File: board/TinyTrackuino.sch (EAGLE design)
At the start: 16 parts, among them M2 HX1, Q1 PMV20XN, PMV16UN, etc, U1 LM60 int, X1 BU-SMA-V, X2 Vin, X3 LM60 ext, X4 Buzzer, X5 SM06B-SRSS-TB

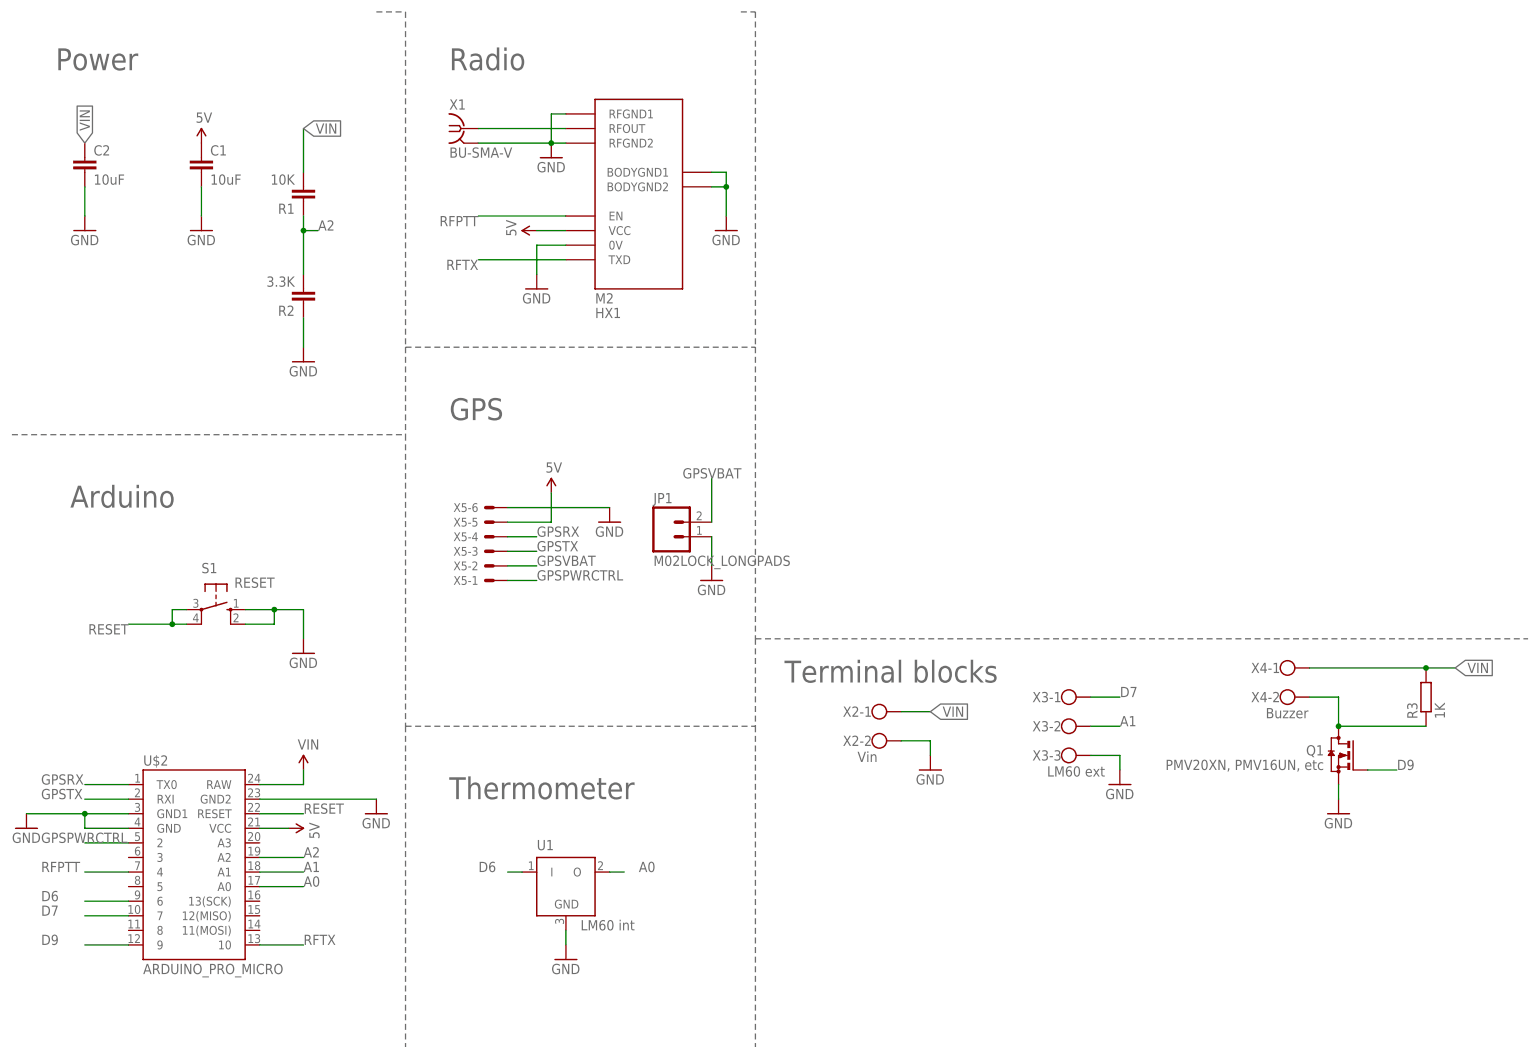
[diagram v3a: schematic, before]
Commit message: Using 3.5mm screw terminals instead of 5mm
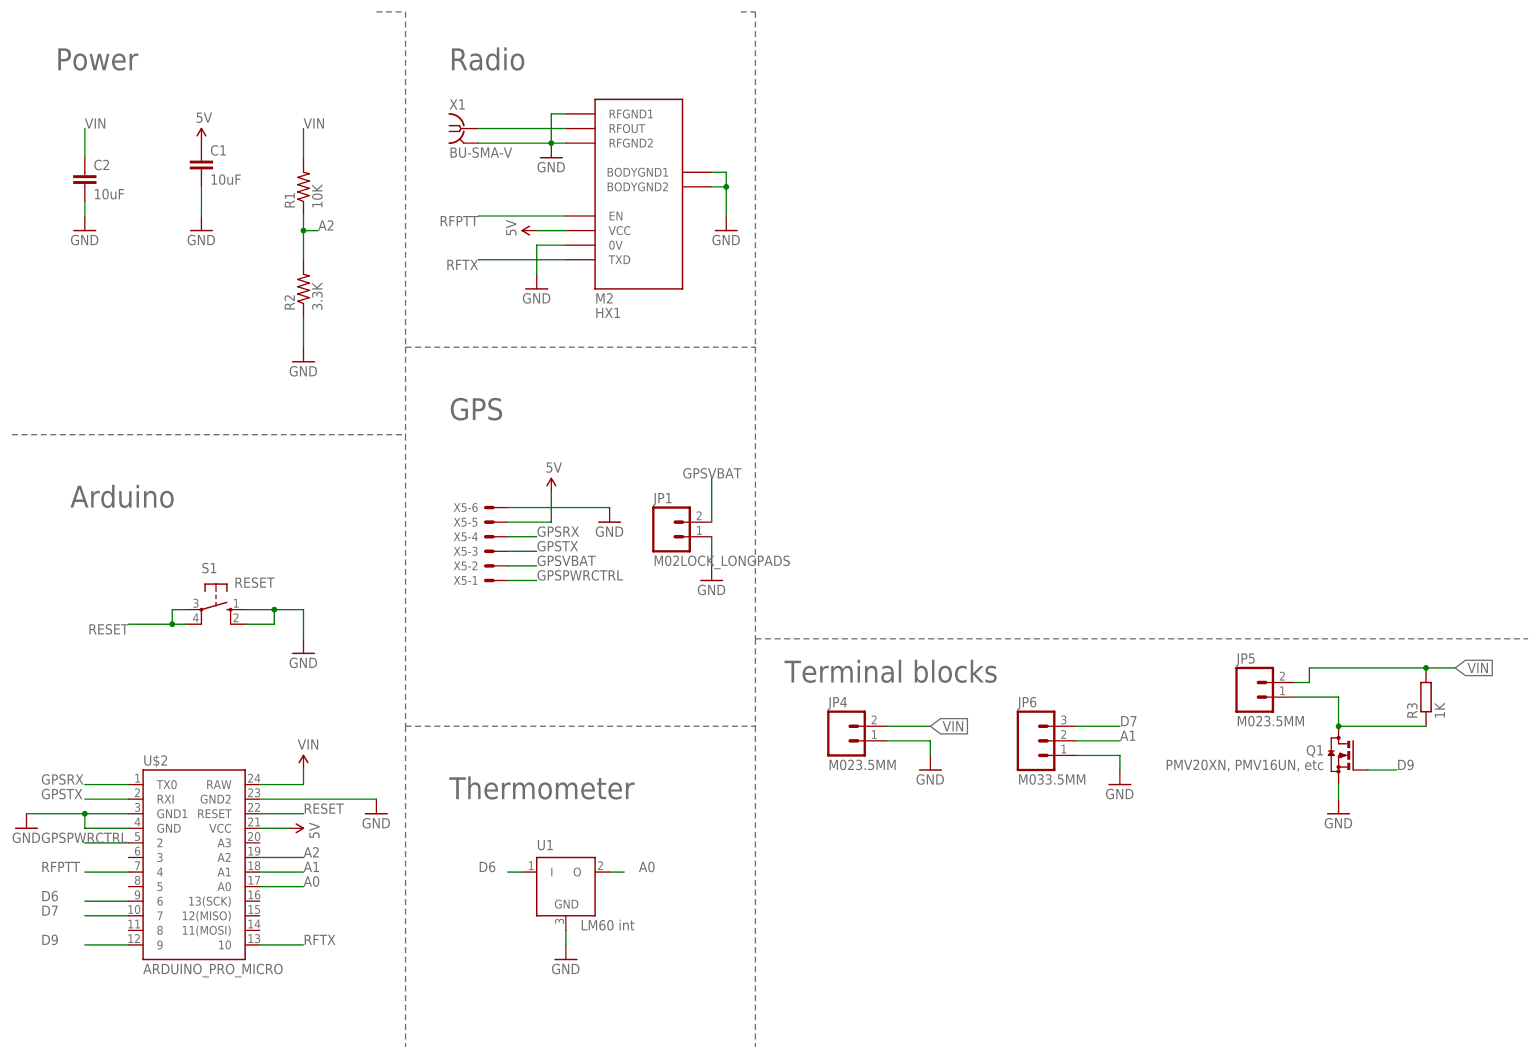
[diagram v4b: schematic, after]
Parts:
- removed X2: Vin, con-wago-500:W237-102
- removed X3: LM60 ext, con-wago-500:W237-103
- removed X4: Buzzer, con-wago-500:W237-102
- added JP4, JP5: M023.5MM, SparkFun-Connectors:M023.5MM
- added JP6: M033.5MM, SparkFun-Connectors:M03SCREW
- R1, R2: device SparkFun-Passives:CAP0603-CAP -> SparkFun-Passives:RESISTOR0603-RES
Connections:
- net A1: now also JP6.2; no longer X3-2.KL
- net D7: now also JP6.3; no longer X3-1.KL
- net GND: now also JP4.1, JP6.1; no longer X2-2.KL, X3-3.KL
- net N$1: now also JP5.1; no longer X4-2.KL
- net VIN: now also JP4.2, JP5.2; no longer X2-1.KL, X4-1.KL
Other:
- moved on the sheet: C2
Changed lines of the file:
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@@
 <part name="U1" library="trackuino" deviceset="LM60" device="" value="LM60 int"/>
 <part name="X1" library="con-coax" deviceset="BU-SMA-V" device=""/>
-<part name="X2" library="con-wago-500" deviceset="W237-102" device="" value="Vin"/>
-<part name="X3" library="con-wago-500" deviceset="W237-103" device="" value="LM60 ext"/>
 <part name="GND12" library="supply1" deviceset="GND" device=""/>
 <part name="GND13" library="supply1" deviceset="GND" device=""/>
-<part name="X4" library="con-wago-500" deviceset="W237-102" device="" value="Buzzer"/>
 <part name="GND14" library="supply1" deviceset="GND" device=""/>
 <part name="GND20" library="supply1" deviceset="GND" device=""/>
-<part name="R1" library="SparkFun-Passives" deviceset="CAP" device="0603-CAP" value="10K"/>
-<part name="R2" library="SparkFun-Passives" deviceset="CAP" device="0603-CAP" value="3.3K"/>
+<part name="R1" library="SparkFun-Passives" deviceset="RESISTOR" device="0603-RES" value="10K"/>
+<part name="R2" library="SparkFun-Passives" deviceset="RESISTOR" device="0603-RES" value="3.3K"/>
 <part name="GND21" library="supply1" deviceset="GND" device=""/>
 <part name="Q1" library="transistor-small-signal" deviceset="BSS123" device="" value="PMV20XN, PMV16UN, etc"/>
@@
 <part name="SUPPLY5" library="SparkFun-Aesthetics" deviceset="5V" device=""/>
 <part name="X5" library="con-jst2" deviceset="?M06B-SRSS-TB" device="S"/>
+<part name="JP4" library="SparkFun-Connectors" deviceset="M02" device="3.5MM"/>
+<part name="JP5" library="SparkFun-Connectors" deviceset="M02" device="3.5MM"/>
+<part name="JP6" library="SparkFun-Connectors" deviceset="M03" device="SCREW" value="M033.5MM"/>
 </parts>
 <sheets>
@@
 <instance part="GND10" gate="1" x="33.02" y="142.24"/>
 <instance part="C1" gate="G$1" x="33.02" y="152.4"/>
-<instance part="C2" gate="G$1" x="12.7" y="152.4"/>
+<instance part="C2" gate="G$1" x="12.7" y="149.86"/>
 <instance part="GND" gate="1" x="93.98" y="154.94"/>
 <instance part="FRAME1" gate="G$1" x="0" y="0"/>
@@
 <instance part="U1" gate="G$1" x="96.52" y="27.94"/>
 <instance part="X1" gate="G$1" x="78.74" y="160.02"/>
-<instance part="X2" gate="-1" x="149.86" y="58.42"/>
-<instance part="X2" gate="-2" x="149.86" y="53.34"/>
-<instance part="X3" gate="-1" x="182.88" y="60.96"/>
-<instance part="X3" gate="-2" x="182.88" y="55.88"/>
-<instance part="X3" gate="-3" x="182.88" y="50.8"/>
 <instance part="GND12" gate="1" x="160.02" y="48.26"/>
 <instance part="GND13" gate="1" x="193.04" y="45.72"/>
-<instance part="X4" gate="-1" x="220.98" y="66.04"/>
-<instance part="X4" gate="-2" x="220.98" y="60.96"/>
 <instance part="GND14" gate="1" x="231.14" y="40.64"/>
 <instance part="GND20" gate="1" x="124.46" y="142.24"/>
-<instance part="R1" gate="G$1" x="50.8" y="149.86" rot="R180"/>
-<instance part="R2" gate="G$1" x="50.8" y="132.08" rot="R180"/>
+<instance part="R1" gate="G$1" x="50.8" y="149.86" rot="R90"/>
+<instance part="R2" gate="G$1" x="50.8" y="132.08" rot="R90"/>
 <instance part="GND21" gate="1" x="50.8" y="119.38"/>
 <instance part="Q1" gate="G$1" x="231.14" y="50.8" rot="MR0"/>
@@
 <instance part="X5" gate="-5" x="83.82" y="91.44" rot="R180"/>
 <instance part="X5" gate="-6" x="83.82" y="93.98" rot="R180"/>
+<instance part="JP4" gate="G$1" x="144.78" y="53.34"/>
+<instance part="JP5" gate="G$1" x="215.9" y="60.96"/>
+<instance part="JP6" gate="G$1" x="177.8" y="53.34"/>
 </instances>
 <busses>
@@
 <net name="GND" class="0">
 <segment>
-<wire x1="12.7" y1="149.86" x2="12.7" y2="144.78" width="0.1524" layer="91"/>
+<wire x1="12.7" y1="147.32" x2="12.7" y2="144.78" width="0.1524" layer="91"/>
 <pinref part="GND9" gate="1" pin="GND"/>
 <pinref part="C2" gate="G$1" pin="2"/>
@@
 </segment>
 <segment>
-<wire x1="154.94" y1="53.34" x2="160.02" y2="53.34" width="0.1524" layer="91"/>
+<wire x1="152.4" y1="53.34" x2="160.02" y2="53.34" width="0.1524" layer="91"/>
 <wire x1="160.02" y1="53.34" x2="160.02" y2="50.8" width="0.1524" layer="91"/>
-<pinref part="X2" gate="-2" pin="KL"/>
 <pinref part="GND12" gate="1" pin="GND"/>
-</segment>
-<segment>
-<wire x1="187.96" y1="50.8" x2="193.04" y2="50.8" width="0.1524" layer="91"/>
+<pinref part="JP4" gate="G$1" pin="1"/>
+</segment>
+<segment>
+<wire x1="185.42" y1="50.8" x2="193.04" y2="50.8" width="0.1524" layer="91"/>
 <wire x1="193.04" y1="50.8" x2="193.04" y2="48.26" width="0.1524" layer="91"/>
-<pinref part="X3" gate="-3" pin="KL"/>
 <pinref part="GND13" gate="1" pin="GND"/>
+<pinref part="JP6" gate="G$1" pin="1"/>
 </segment>
 <segment>
@@
 <net name="VIN" class="0">
 <segment>
-<wire x1="154.94" y1="58.42" x2="160.02" y2="58.42" width="0.1524" layer="91"/>
-<label x="160.02" y="58.42" size="1.778" layer="95" xref="yes"/>
-<pinref part="X2" gate="-1" pin="KL"/>
-</segment>
-<segment>
-<wire x1="50.8" y1="152.4" x2="50.8" y2="160.02" width="0.1524" layer="91"/>
-<label x="50.8" y="160.02" size="1.778" layer="95" xref="yes"/>
-<pinref part="R1" gate="G$1" pin="2"/>
+<wire x1="152.4" y1="55.88" x2="160.02" y2="55.88" width="0.1524" layer="91"/>
+<label x="160.02" y="55.88" size="1.778" layer="95" xref="yes"/>
+<pinref part="JP4" gate="G$1" pin="2"/>
 </segment>
 <segment>
@@
 <junction x="246.38" y="66.04"/>
 <label x="251.46" y="66.04" size="1.778" layer="95" xref="yes"/>
-<pinref part="X4" gate="-1" pin="KL"/>
 <pinref part="R3" gate="G$1" pin="2"/>
-</segment>
-<segment>
-<pinref part="C2" gate="G$1" pin="1"/>
-<label x="12.7" y="157.48" size="1.778" layer="95" rot="R90" xref="yes"/>
+<pinref part="JP5" gate="G$1" pin="2"/>
+<wire x1="223.52" y1="63.5" x2="226.06" y2="63.5" width="0.1524" layer="91"/>
+<wire x1="226.06" y1="63.5" x2="226.06" y2="66.04" width="0.1524" layer="91"/>
 </segment>
 <segment>
@@
 <wire x1="50.8" y1="45.72" x2="50.8" y2="48.26" width="0.1524" layer="91"/>
 </segment>
+<segment>
+<pinref part="C2" gate="G$1" pin="1"/>
+<wire x1="12.7" y1="160.02" x2="12.7" y2="154.94" width="0.1524" layer="91"/>
+<label x="12.7" y="160.02" size="1.778" layer="95"/>
+</segment>
+<segment>
+<pinref part="R1" gate="G$1" pin="2"/>
+<wire x1="50.8" y1="154.94" x2="50.8" y2="160.02" width="0.1524" layer="91"/>
+<label x="50.8" y="160.02" size="1.778" layer="95"/>
+</segment>
 </net>
 <net name="A0" class="0">
@@
 <net name="A1" class="0">
 <segment>
-<wire x1="187.96" y1="55.88" x2="193.04" y2="55.88" width="0.1524" layer="91"/>
-<label x="193.04" y="55.88" size="1.778" layer="95"/>
-<pinref part="X3" gate="-2" pin="KL"/>
+<wire x1="185.42" y1="53.34" x2="193.04" y2="53.34" width="0.1524" layer="91"/>
+<label x="193.04" y="53.34" size="1.778" layer="95"/>
+<pinref part="JP6" gate="G$1" pin="2"/>
 </segment>
 <segment>
@@
 <segment>
 <wire x1="50.8" y1="144.78" x2="50.8" y2="142.24" width="0.1524" layer="91"/>
-<wire x1="50.8" y1="142.24" x2="50.8" y2="134.62" width="0.1524" layer="91"/>
+<wire x1="50.8" y1="142.24" x2="50.8" y2="137.16" width="0.1524" layer="91"/>
 <wire x1="50.8" y1="142.24" x2="53.34" y2="142.24" width="0.1524" layer="91"/>
 <junction x="50.8" y="142.24"/>
@@
 <net name="D7" class="0">
 <segment>
-<wire x1="187.96" y1="60.96" x2="193.04" y2="60.96" width="0.1524" layer="91"/>
-<label x="193.04" y="60.96" size="1.778" layer="95"/>
-<pinref part="X3" gate="-1" pin="KL"/>
+<wire x1="185.42" y1="55.88" x2="193.04" y2="55.88" width="0.1524" layer="91"/>
+<label x="193.04" y="55.88" size="1.778" layer="95"/>
+<pinref part="JP6" gate="G$1" pin="3"/>
 </segment>
 <segment>
@@
 <net name="N$1" class="0">
 <segment>
-<wire x1="226.06" y1="60.96" x2="231.14" y2="60.96" width="0.1524" layer="91"/>
+<wire x1="223.52" y1="60.96" x2="231.14" y2="60.96" width="0.1524" layer="91"/>
 <wire x1="231.14" y1="60.96" x2="231.14" y2="55.88" width="0.1524" layer="91"/>
 <wire x1="231.14" y1="55.88" x2="246.38" y2="55.88" width="0.1524" layer="91"/>
 <junction x="231.14" y="55.88"/>
-<pinref part="X4" gate="-2" pin="KL"/>
 <pinref part="Q1" gate="G$1" pin="D"/>
 <pinref part="R3" gate="G$1" pin="1"/>
-</segment>
-</net>
+<pinref part="JP5" gate="G$1" pin="1"/>
+</segment>
+</net>

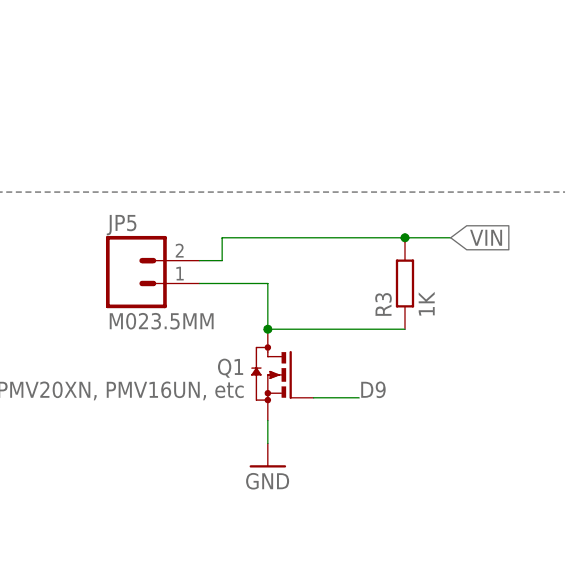
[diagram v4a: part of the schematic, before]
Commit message: Moving Vin to edge of board
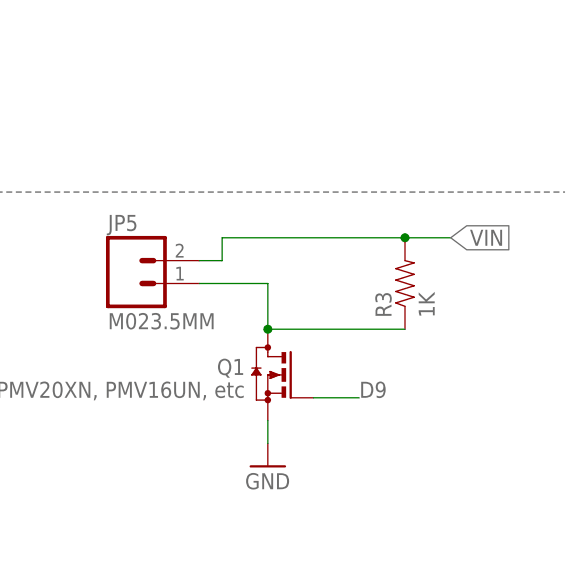
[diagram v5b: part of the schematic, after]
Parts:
- R3: device resistor:R-EU_R1206 -> SparkFun-Passives:RESISTOR0603-RES
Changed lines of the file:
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@@
 <part name="GND21" library="supply1" deviceset="GND" device=""/>
 <part name="Q1" library="transistor-small-signal" deviceset="BSS123" device="" value="PMV20XN, PMV16UN, etc"/>
-<part name="R3" library="resistor" deviceset="R-EU_" device="R1206" value="1K"/>
+<part name="R3" library="SparkFun-Passives" deviceset="RESISTOR" device="0603-RES" value="1K"/>
 <part name="U$2" library="SparkFun-Boards" deviceset="ARDUINO_PRO_MICRO" device=""/>
 <part name="SUPPLY2" library="SparkFun-Aesthetics" deviceset="VIN" device=""/>
